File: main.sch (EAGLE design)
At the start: 27 parts, among them IC1 SN754410, IC2 7805T, T1 BPX81, T2 BPX81, T3 BPX81, T4 BPX81

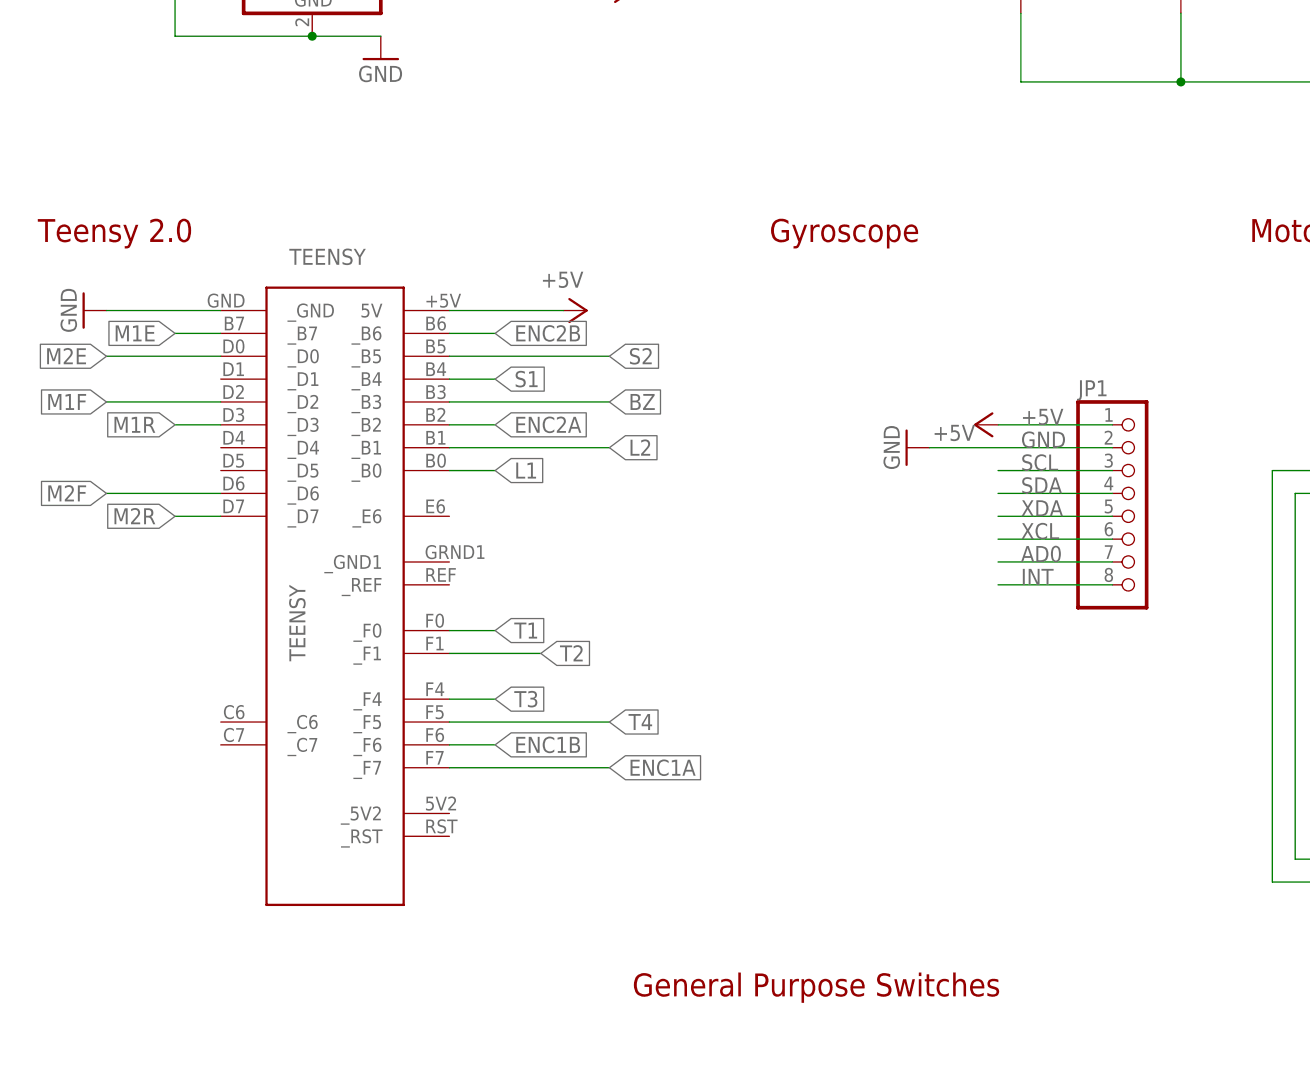
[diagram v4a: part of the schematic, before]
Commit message: Removed gyroscope
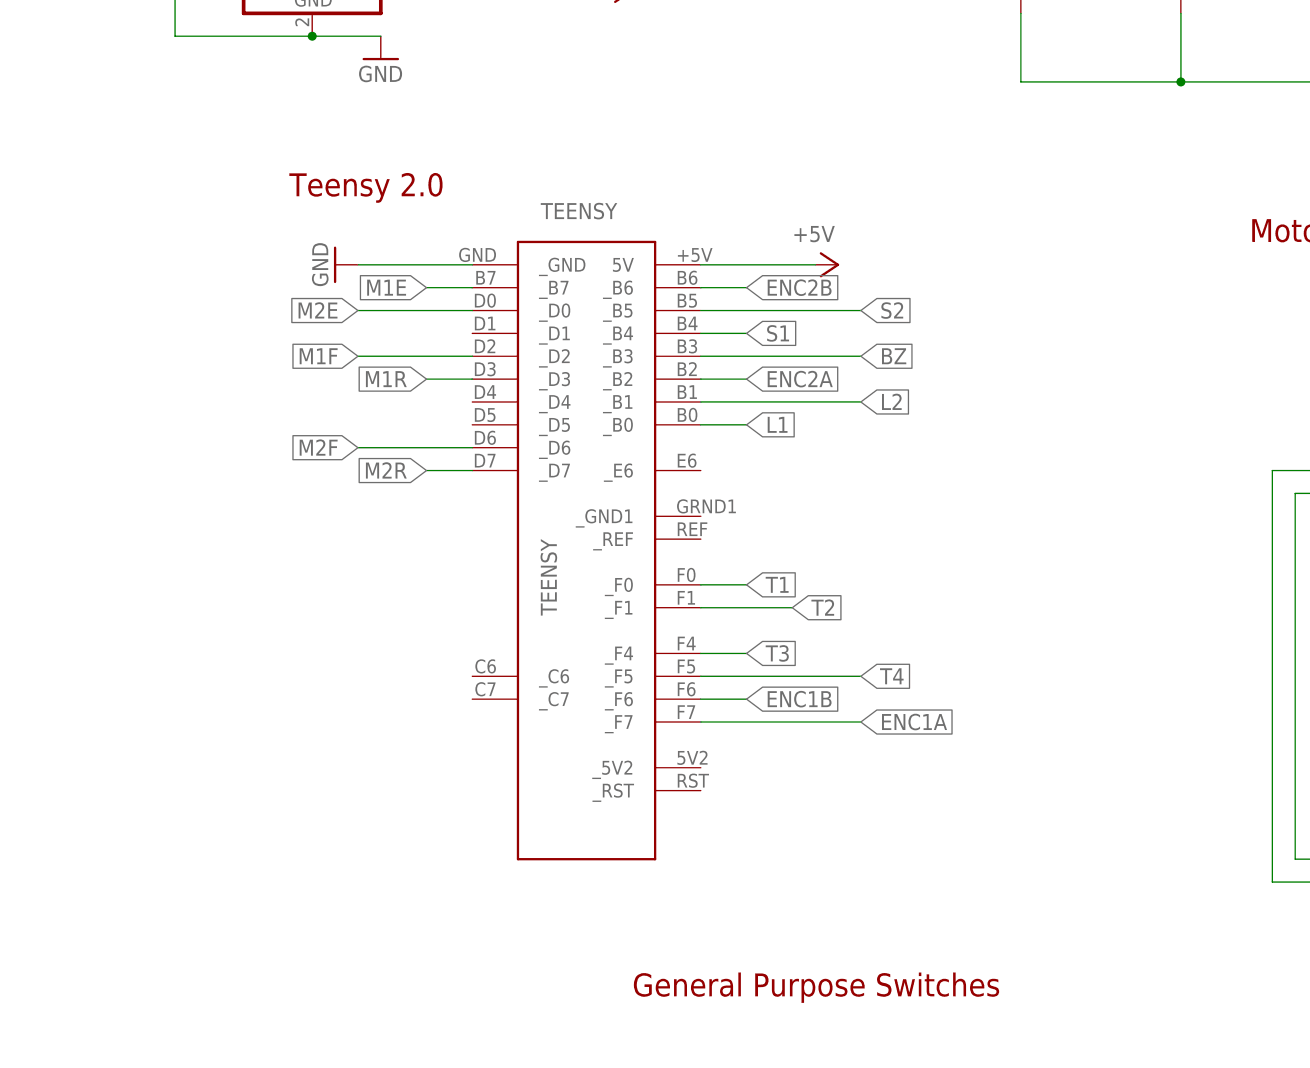
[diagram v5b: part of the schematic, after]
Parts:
- removed JP1: (no value), pinhead:PINHD-1X8
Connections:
- removed net AD0: JP1.7
- removed net INT: JP1.8
- removed net SCL: JP1.3
- removed net SDA: JP1.4
- removed net XCL: JP1.6
- removed net XDA: JP1.5
- net +5V: no longer JP1.1
- net GND: no longer JP1.2
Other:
- note removed: "Gyroscope"
- moved on the sheet: TEENSY

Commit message: Updated motor
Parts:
- added U$1, U$2: POLULUMOTOR, personal:POLULUMOTOR
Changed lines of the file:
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@@
 <part name="S3" library="switch" library_urn="urn:adsk.eagle:library:380" deviceset="255SB" device="" package3d_urn="urn:adsk.eagle:package:27679/1"/>
 <part name="P+8" library="supply1" library_urn="urn:adsk.eagle:library:371" deviceset="+5V" device=""/>
+<part name="U$1" library="personal" deviceset="POLULUMOTOR" device=""/>
+<part name="U$2" library="personal" deviceset="POLULUMOTOR" device=""/>
 </parts>
 <sheets>
@@
 <attribute name="VALUE" x="76.2" y="167.64" size="1.778" layer="96"/>
 </instance>
+<instance part="U$1" gate="G$1" x="12.7" y="15.24" smashed="yes"/>
+<instance part="U$2" gate="G$1" x="12.7" y="10.16" smashed="yes"/>
 </instances>
 <busses>

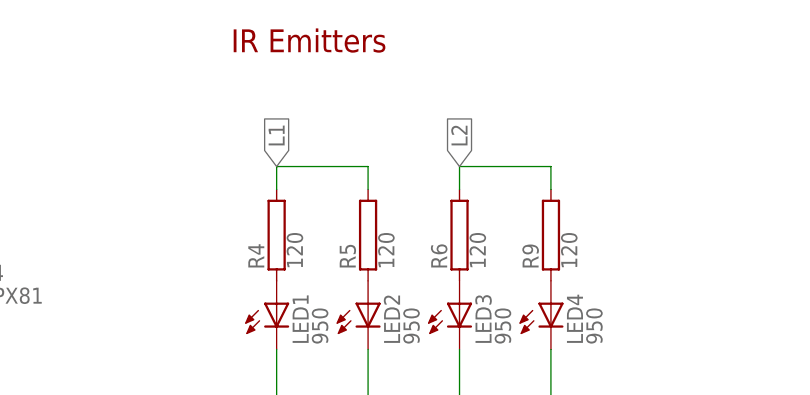
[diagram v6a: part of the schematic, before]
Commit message: Updated LED Wiring
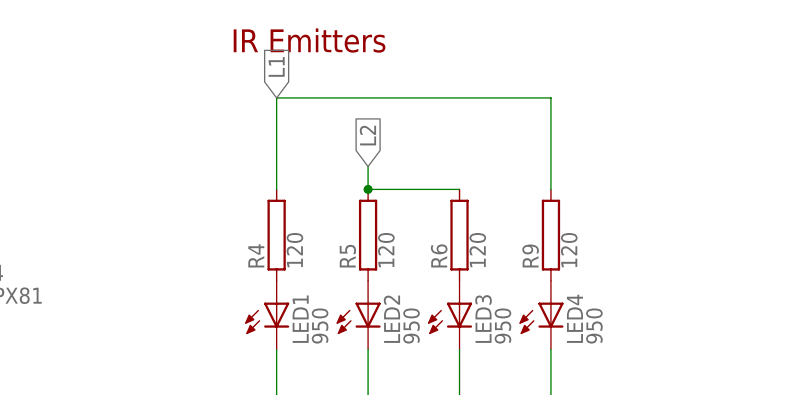
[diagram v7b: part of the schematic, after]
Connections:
- net L1: now also R9.2; no longer R5.2
- net L2: now also R5.2; no longer R9.2
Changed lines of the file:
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@@
 <net name="L1" class="0">
 <segment>
-<wire x1="213.36" y1="180.34" x2="213.36" y2="182.88" width="0.1524" layer="91"/>
-<label x="213.36" y="182.88" size="1.778" layer="95" rot="R90" xref="yes"/>
+<wire x1="213.36" y1="180.34" x2="213.36" y2="190.5" width="0.1524" layer="91"/>
+<label x="213.36" y="190.5" size="1.778" layer="95" rot="R90" xref="yes"/>
 <pinref part="R4" gate="G$1" pin="2"/>
-<wire x1="213.36" y1="182.88" x2="223.52" y2="182.88" width="0.1524" layer="91"/>
-<pinref part="R5" gate="G$1" pin="2"/>
-<wire x1="223.52" y1="182.88" x2="223.52" y2="180.34" width="0.1524" layer="91"/>
+<pinref part="R9" gate="G$1" pin="2"/>
+<wire x1="213.36" y1="190.5" x2="243.84" y2="190.5" width="0.1524" layer="91"/>
+<wire x1="243.84" y1="190.5" x2="243.84" y2="180.34" width="0.1524" layer="91"/>
 </segment>
 <segment>
@@
 </segment>
 <segment>
-<wire x1="233.68" y1="180.34" x2="233.68" y2="182.88" width="0.1524" layer="91"/>
+<label x="223.52" y="182.88" size="1.778" layer="95" rot="R90" xref="yes"/>
+<pinref part="R5" gate="G$1" pin="2"/>
+<wire x1="223.52" y1="182.88" x2="223.52" y2="180.34" width="0.1524" layer="91"/>
 <pinref part="R6" gate="G$1" pin="2"/>
-<label x="233.68" y="182.88" size="1.778" layer="95" rot="R90" xref="yes"/>
-<pinref part="R9" gate="G$1" pin="2"/>
-<wire x1="243.84" y1="180.34" x2="243.84" y2="182.88" width="0.1524" layer="91"/>
-<wire x1="233.68" y1="182.88" x2="243.84" y2="182.88" width="0.1524" layer="91"/>
+<wire x1="233.68" y1="180.34" x2="223.52" y2="180.34" width="0.1524" layer="91"/>
+<junction x="223.52" y="180.34"/>
 </segment>
 </net>

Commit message: Peer Review Version
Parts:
- added U$3: CASTERBALL, personal:CASTERBALL
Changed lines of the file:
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@@
 <part name="S3" library="switch" library_urn="urn:adsk.eagle:library:380" deviceset="255SB" device="" package3d_urn="urn:adsk.eagle:package:27679/1"/>
 <part name="P+8" library="supply1" library_urn="urn:adsk.eagle:library:371" deviceset="+5V" device=""/>
+<part name="U$3" library="personal" deviceset="CASTERBALL" device=""/>
+<part name="U$2" library="personal" deviceset="POLULUMOTOR" device=""/>
 <part name="U$1" library="personal" deviceset="POLULUMOTOR" device=""/>
-<part name="U$2" library="personal" deviceset="POLULUMOTOR" device=""/>
 </parts>
 <sheets>
@@
 <attribute name="VALUE" x="76.2" y="167.64" size="1.778" layer="96"/>
 </instance>
+<instance part="U$3" gate="G$1" x="12.7" y="5.08" smashed="yes"/>
+<instance part="U$2" gate="G$1" x="12.7" y="10.16" smashed="yes"/>
 <instance part="U$1" gate="G$1" x="12.7" y="15.24" smashed="yes"/>
-<instance part="U$2" gate="G$1" x="12.7" y="10.16" smashed="yes"/>
 </instances>
 <busses>
